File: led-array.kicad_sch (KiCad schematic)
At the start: 42 parts, among them J1 Conn_01x04_Pin, J2 USB_B_Micro, Q1 Q_NMOS_GDS, Q2 Q_NMOS_GDS, Q3 Q_NMOS_GDS, Q4 Q_NMOS_GDS, Q5 Q_NMOS_GDS, Q6 Q_NMOS_GDS, Q7 Q_NMOS_GDS, Q8 Q_NMOS_GDS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

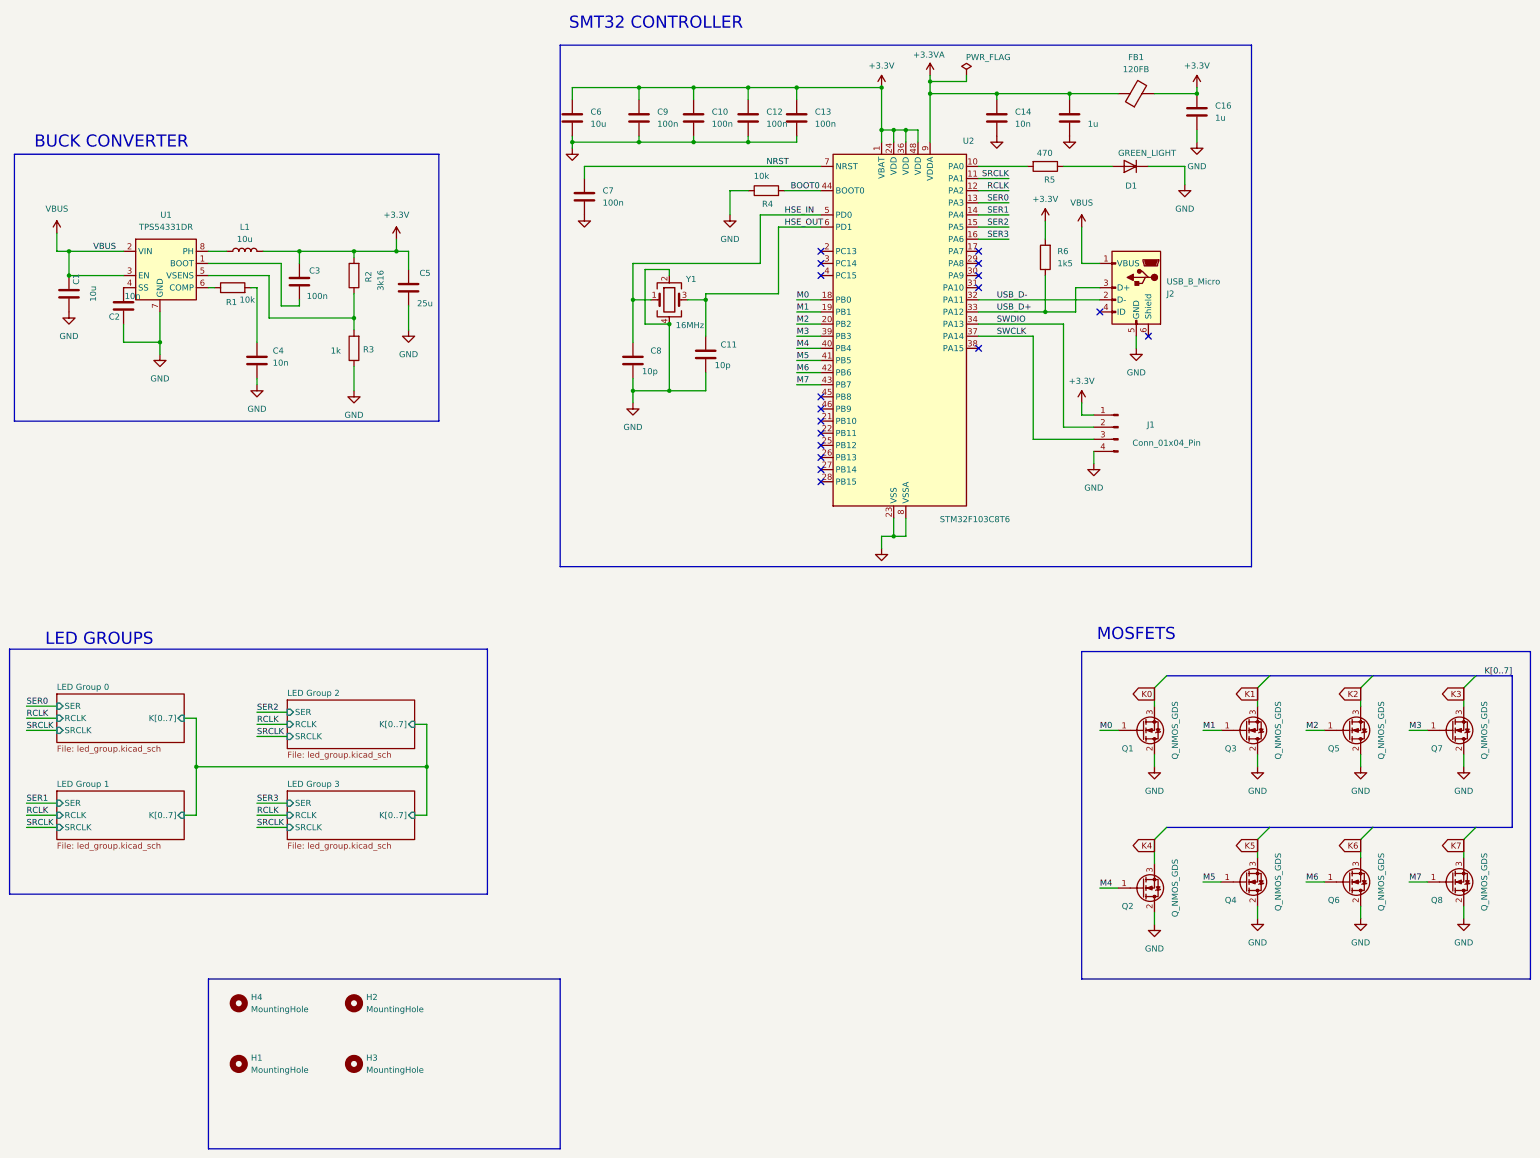
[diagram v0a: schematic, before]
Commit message: Updated schematic, still likely need to modify the buck converter
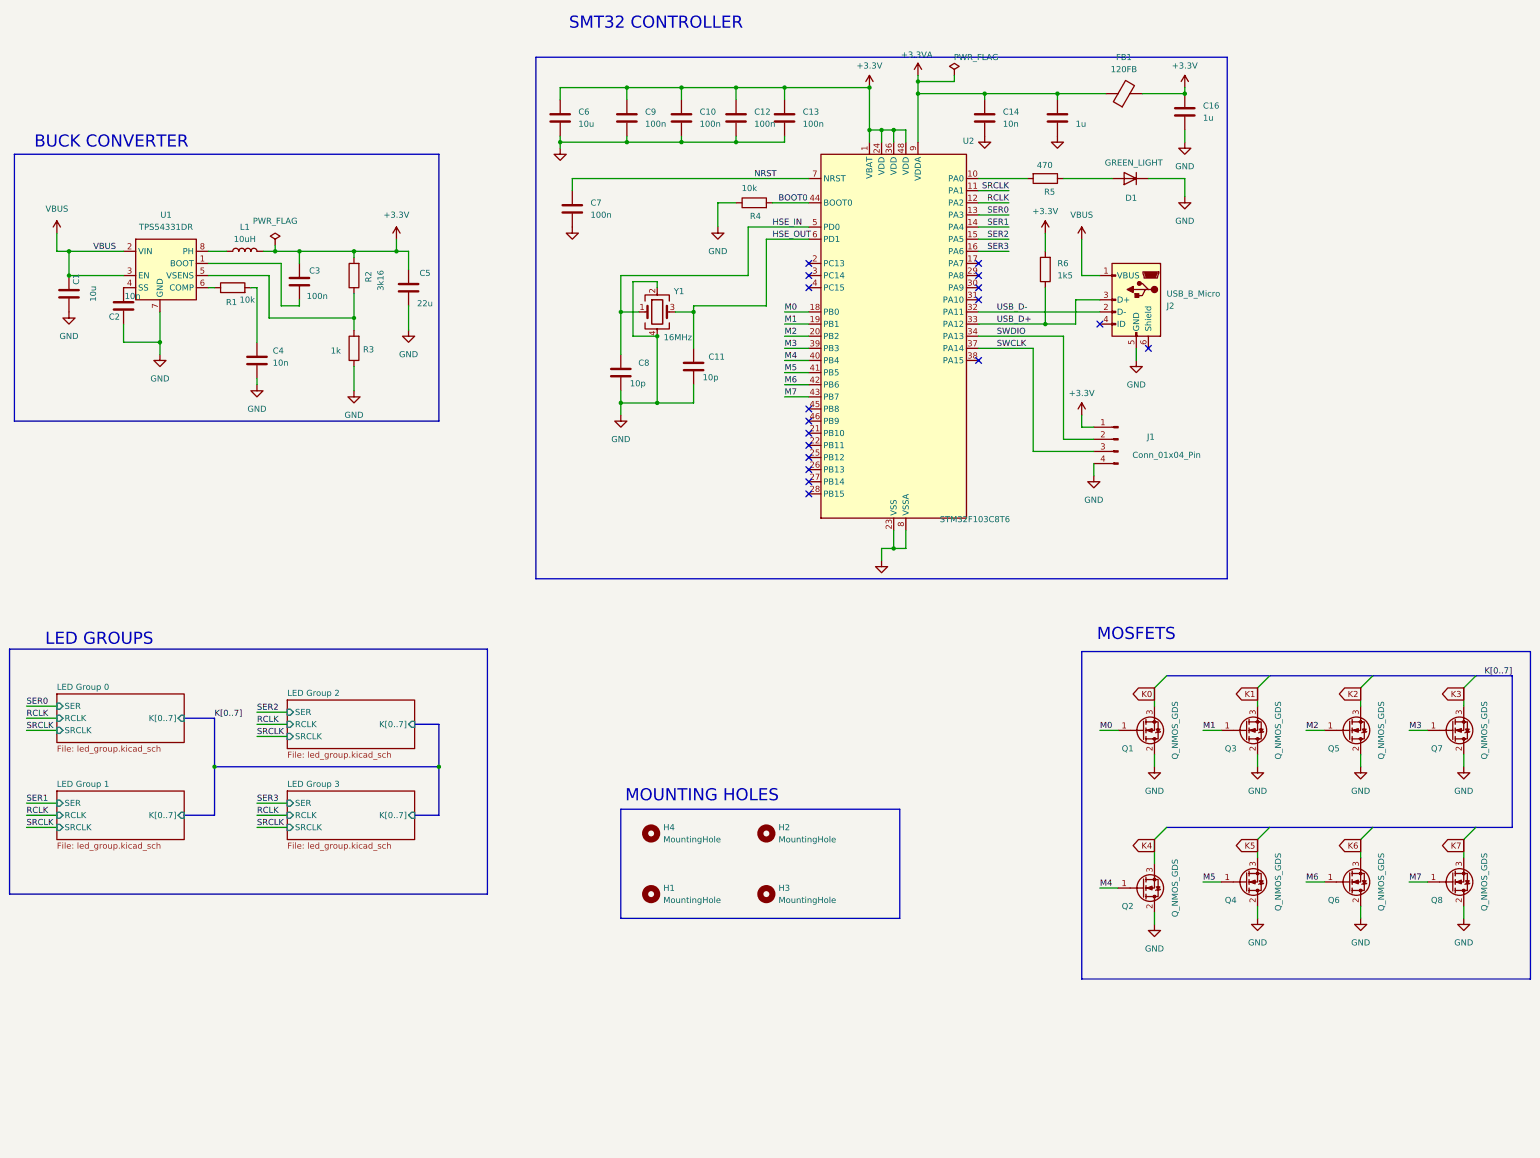
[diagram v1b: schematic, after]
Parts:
- C5: value 25u -> 22u
- L1: value 10u -> 10uH
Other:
- note added: "MOUNTING HOLES"
- moved on the sheet: C10, C11, C12, C13, C14, C16, C6, C7, C8, C9, D1, FB1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

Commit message: Modified buck converter in schematic and pcb and got rid of old fabrication files
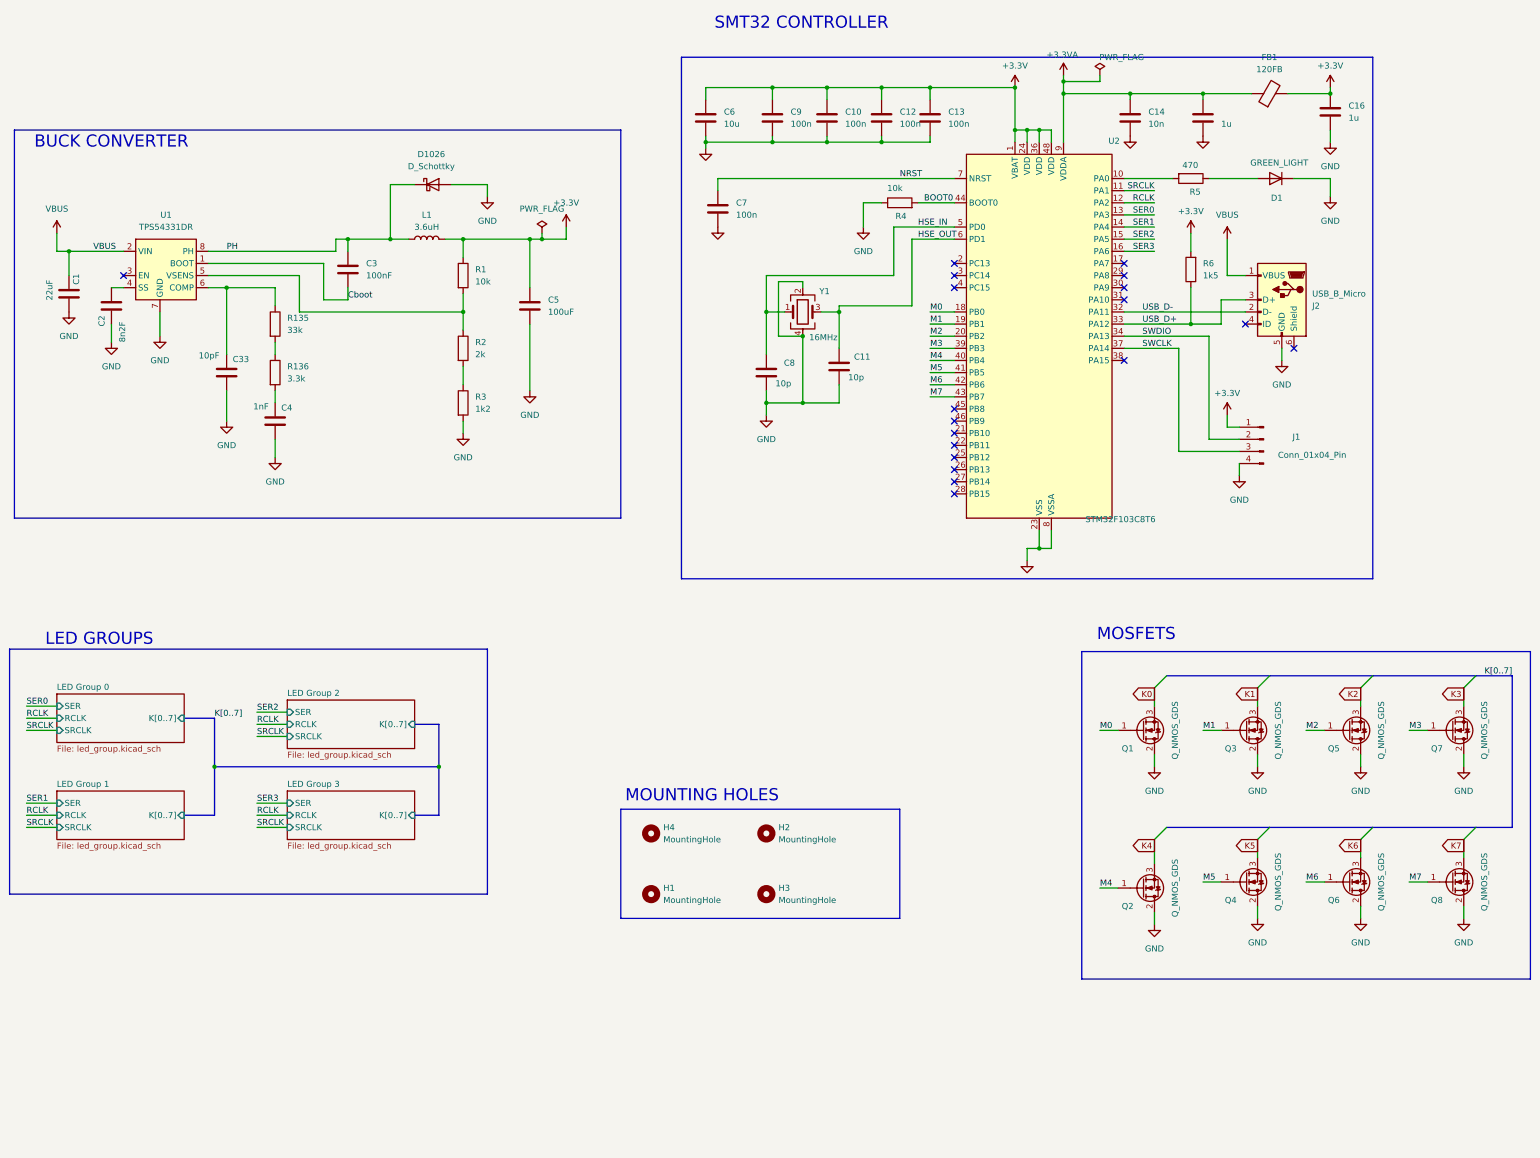
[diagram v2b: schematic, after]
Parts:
- added C33: 10pF, Capacitor_SMD:C_0603_1608Metric, symbol Device:C
- added D1026: D_Schottky, Diode_SMD:D_SMA, symbol Device:D_Schottky
- added R135: 33k, Resistor_SMD:R_0402_1005Metric, symbol Device:R
- added R136: 3.3k, Resistor_SMD:R_0402_1005Metric, symbol Device:R
- C1: value 10u -> 22uF; footprint Capacitor_SMD:C_0603_1608Metric -> Capacitor_SMD:C_1206_3216Metric; LCSC (none) -> C12891
- C10, C12, C13, C7, C9: LCSC (none) -> C1525
- C2: value 10n -> 8n2F; footprint Capacitor_SMD:C_0402_1005Metric -> Capacitor_SMD:C_0603_1608Metric; LCSC (none) -> C1322360
- C3: value 100n -> 100nF; LCSC (none) -> C1525
- C4: value 10n -> 1nF; LCSC (none) -> C1523
- C5: value 22u -> 100uF; footprint Capacitor_SMD:C_0805_2012Metric -> Capacitor_SMD:C_1206_3216Metric; LCSC (none) -> C15008
- L1: value 10uH -> 3.6uH; footprint Inductor_SMD:L_6.3x6.3_H3 -> Inductor_SMD:L_Bourns-SRN8040_8x8.15mm; LCSC (none) -> C6496151
- R1: footprint Resistor_SMD:R_0402_1005Metric -> Resistor_SMD:R_0805_2012Metric; LCSC (none) -> C17414
- R2: value 3k16 -> 2k; LCSC (none) -> C4109
- R3: value 1k -> 1k2; footprint Resistor_SMD:R_0402_1005Metric -> Resistor_SMD:R_0603_1608Metric; LCSC (none) -> C22765
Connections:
- net +3.3V: now also R1.1; no longer C3.1, R2.2
- net GND: now also R3.2, C33.2, D1026.2 (A); no longer R3.1
- net VBUS: no longer U1.3 (EN)
- net at U1.6 (COMP): now also C33.1, R135.1; no longer R1.1
- net at R1.2: now also R2.1, U1.5 (VSENS); no longer C4.1
- net Cboot: now reaches C3.2, U1.1 (BOOT)
- net PH: now reaches L1.1, U1.8 (PH)
- net PH: now also C3.1, D1026.1 (K)
- new net: C4.1, R136.2
- new net: R2.2, R3.1
- new net: R135.2, R136.1
- no-connect marks 18 -> 19
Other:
- moved on the sheet: C10, C11, C12, C13, C14, C16, C2, C6, C7, C8, C9, D1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

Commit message: Updated usb-micro, have filled in all LCSC fields
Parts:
- C10, C12, C13, C7, C9: value 100n -> 100nF; LCSC C1525 -> C1525
- C11, C8: value 10p -> 10pF; LCSC (none) -> C32949
- C14: value 10n -> 10nF; LCSC (none) -> C57112
- C15, C16: value 1u -> 1uF; footprint Capacitor_SMD:C_0402_1005Metric -> Capacitor_SMD:C_0603_1608Metric; LCSC (none) -> C15849
- C33: footprint Capacitor_SMD:C_0603_1608Metric -> Capacitor_SMD:C_0402_1005Metric; LCSC C1634 -> C32949
- C6: value 10u -> 10uF; footprint Capacitor_SMD:C_0603_1608Metric -> Capacitor_SMD:C_1206_3216Metric; LCSC (none) -> C13585
- D1: footprint LED_SMD:LED_1206_3216Metric -> LED_SMD:LED_0805_2012Metric; LCSC (none) -> C2297
- FB1: LCSC (none) -> C14709
- J1: LCSC (none) -> C5116483
- J2: footprint Connector_USB:USB_Micro-B_Wuerth_629105150521 -> Connector_USB:USB_Micro-B_Molex-105017-0001; LCSC (none) -> C136000
- Q1, Q2, Q3, Q4, Q5, Q6, Q7, Q8: LCSC (none) -> C8545
- R4: footprint Resistor_SMD:R_0402_1005Metric -> Resistor_SMD:R_0805_2012Metric; LCSC (none) -> C17414
- R5: LCSC (none) -> C25117
- R6: footprint Resistor_SMD:R_0402_1005Metric -> Resistor_SMD:R_0603_1608Metric; LCSC (none) -> C22843
- U1: LCSC (none) -> C9865
- U2: LCSC (none) -> C8734
- Y1: LCSC (none) -> C9002
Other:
- note added: "C1525"
